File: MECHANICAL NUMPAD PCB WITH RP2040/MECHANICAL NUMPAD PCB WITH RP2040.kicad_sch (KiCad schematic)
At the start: 71 parts, among them IC2 RP2040_QFN56, J1 USB_C_Receptacle_USB2.0_16P, SW1 SW_Push, SW10 SW_Push, SW11 SW_Push, SW12 SW_Push, SW13 SW_Push, SW14 SW_Push, SW15 SW_Push, SW16 SW_Push, SW17 SW_Push, SW2 SW_Push, SW21 SKRAAKE010, SW22 SKRAAKE010, SW3 SW_Push, SW4 SW_Push, SW5 SW_Push, SW6 SW_Push, SW7 SW_Push, SW8 SW_Push, SW9 SW_Push, U2 AP2112K-3.3, U5 8MB QSPI Flash, Y1 12MHZ

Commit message: Finished PCB
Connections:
- net ROW1: now also D4.1 (K)
- net ROW2: no longer D10.1 (K), D11.1 (K), D12.1 (K), D13.1 (K), D14.1 (K), D15.1 (K), D16.1 (K), D17.1 (K), D9.1 (K)
- net ROW3: now also D10.1 (K), D11.1 (K), D12.1 (K), D9.1 (K)
- net ROW4: now also D13.1 (K), D14.1 (K), D15.1 (K), D16.1 (K)
- net ROW5: now also D17.1 (K)
- net at D4.2 (A): now also SW4.2
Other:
- moved on the sheet: C10, C11, C12, C13, C14, C15, C16, C17, C19, C20, C7, C9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

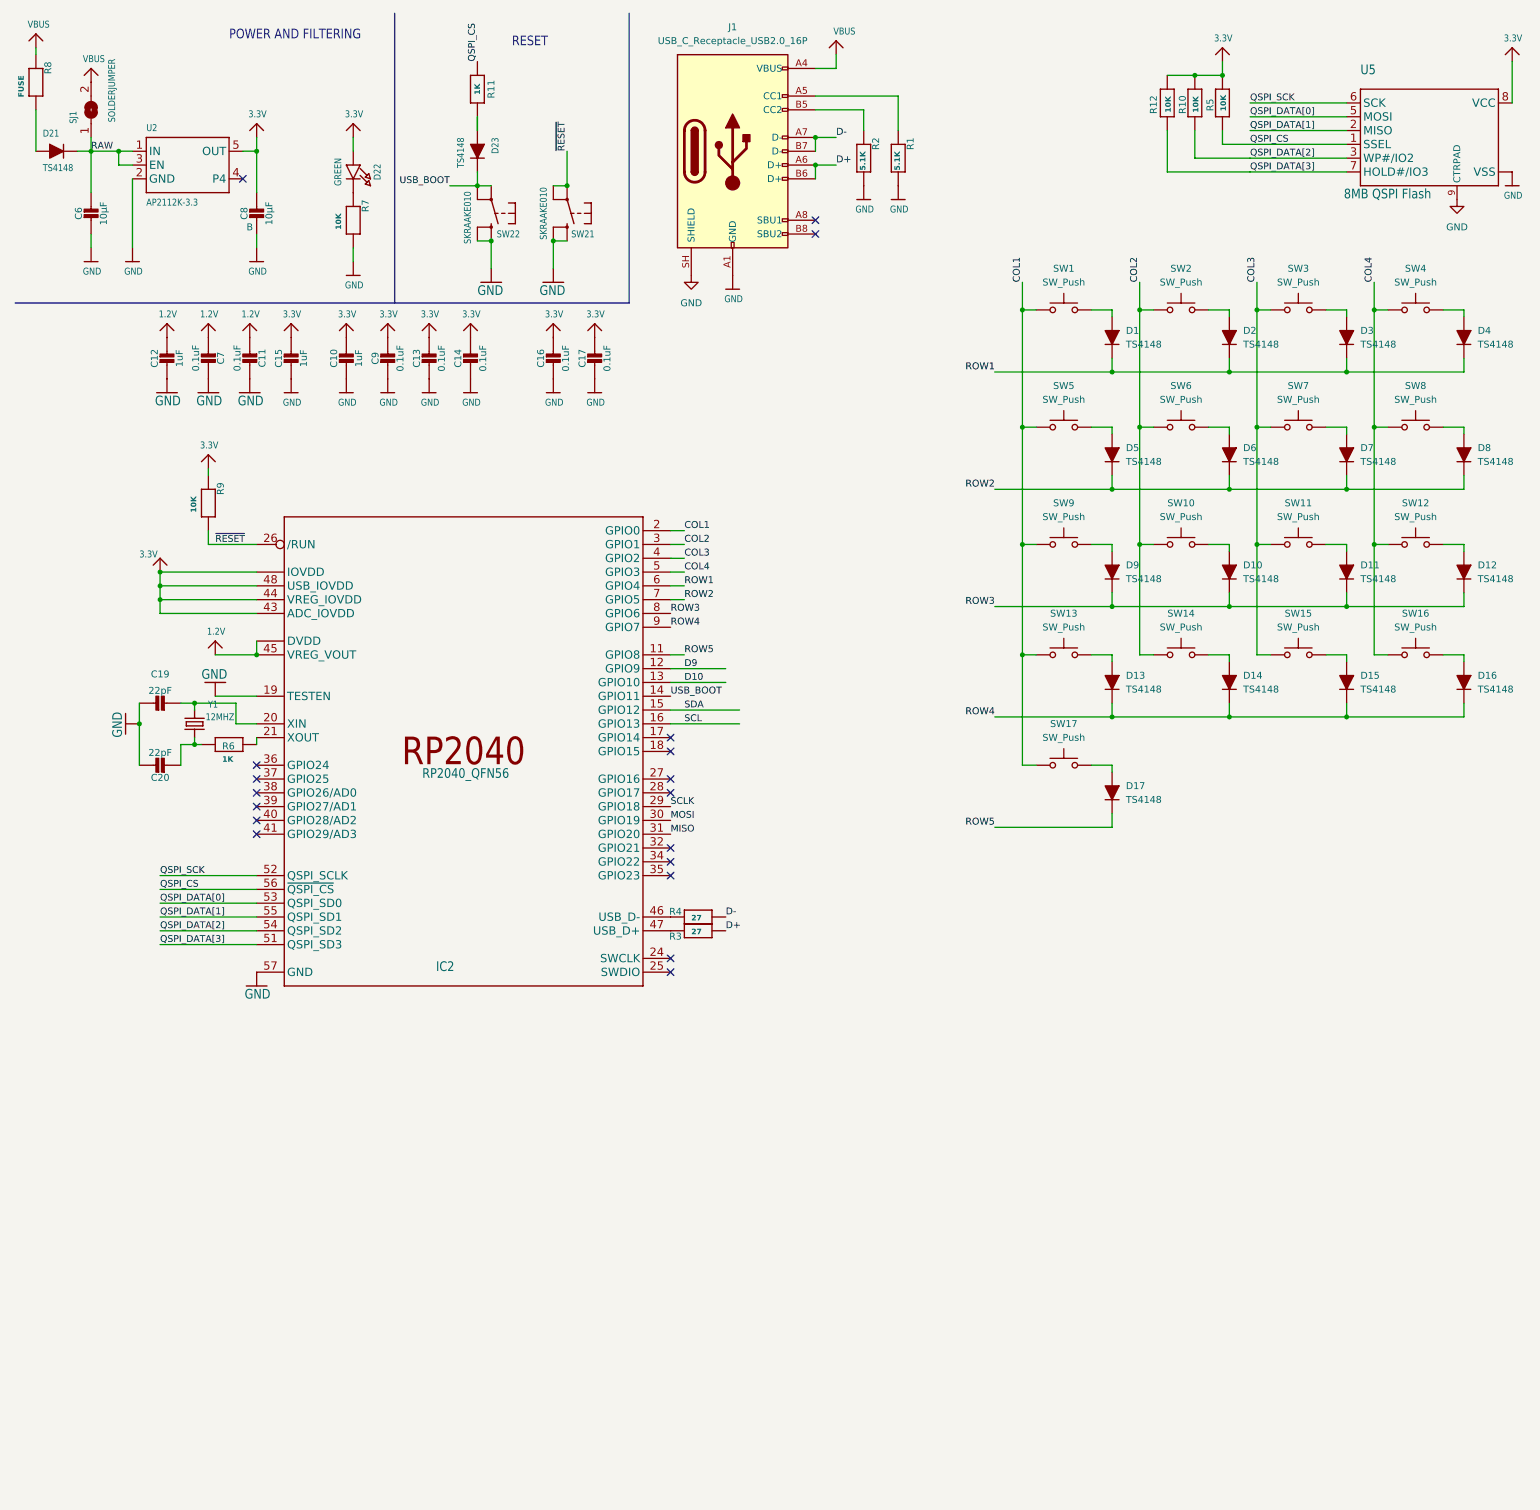
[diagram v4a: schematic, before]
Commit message: In progress of adding Neopixels
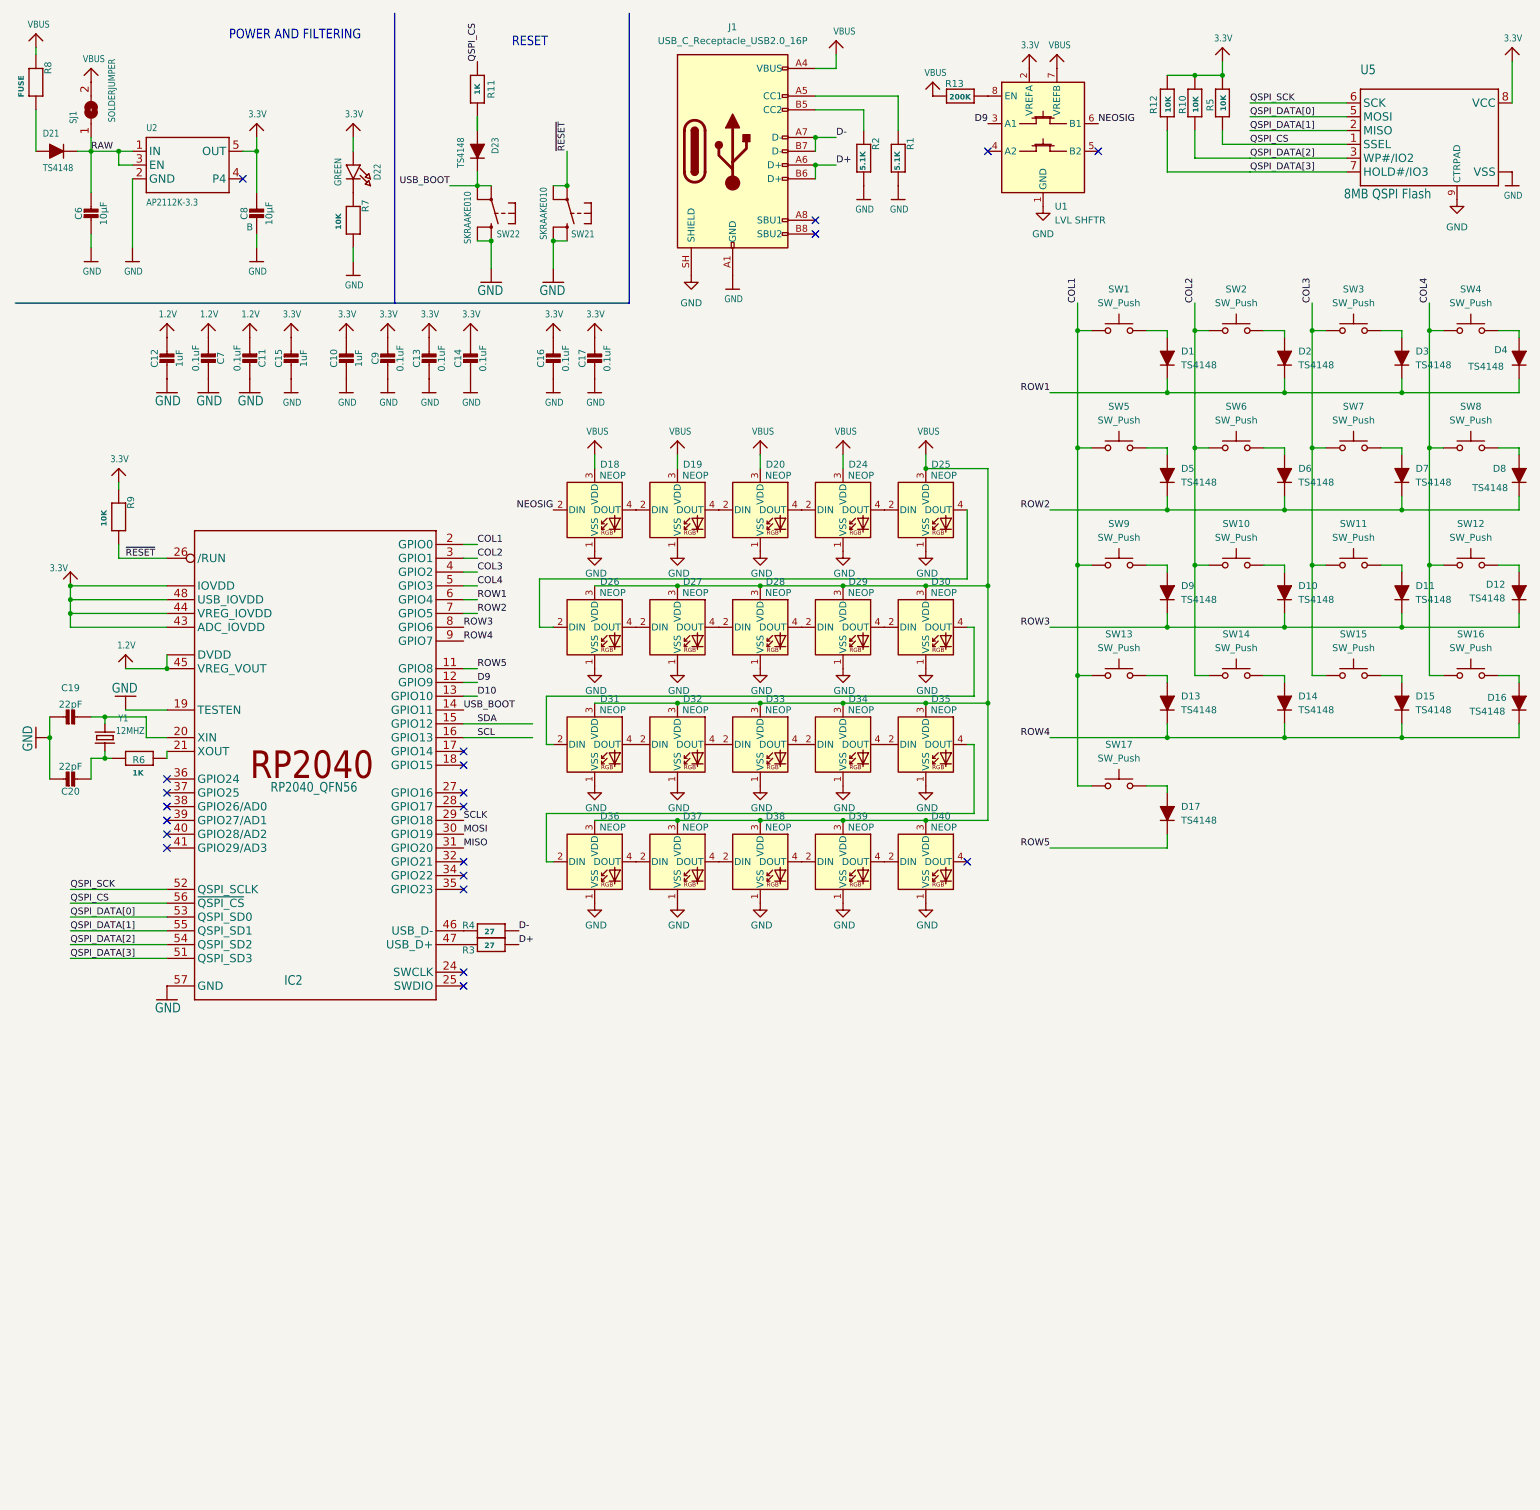
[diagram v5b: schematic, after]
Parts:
- added D18, D19, D20, D24, D25, D26, D27, D28, D29, D30, D31, D32, D33, D34, D35, D36, D37, D38, D39, D40: NEOP, LED_SMD:LED_SK6812MINI-E_3.2x2.8mm_P1.5mm_ReverseMount, symbol LED:SK6812MINI-E
- added R13: 200K, Resistor_SMD:R_0603_1608Metric, symbol Adafruit KB2040-eagle-import:RESISTOR_0402NO
- added U1: LVL SHFTR, Package_SO:VSSOP-8_2.3x2mm_P0.5mm, symbol Logic_LevelTranslator:TXS0102DCU
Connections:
- net 3.3V: now also U1.2 (VREFA)
- net D9: now also U1.3 (A1)
- net GND: now also D18.1 (VSS), D19.1 (VSS), D20.1 (VSS), D24.1 (VSS), D25.1 (VSS), D26.1 (VSS), D27.1 (VSS), D28.1 (VSS), D29.1 (VSS), D30.1 (VSS), D31.1 (VSS), D32.1 (VSS), D33.1 (VSS), D34.1 (VSS), D35.1 (VSS), D36.1 (VSS), D37.1 (VSS), D38.1 (VSS), D39.1 (VSS), D40.1 (VSS), U1.1 (GND)
- net VBUS: now also D18.3 (VDD), D19.3 (VDD), D20.3 (VDD), D24.3 (VDD), D25.3 (VDD), D26.3 (VDD), D27.3 (VDD), D28.3 (VDD), D29.3 (VDD), D30.3 (VDD), D31.3 (VDD), D32.3 (VDD), D33.3 (VDD), D34.3 (VDD), D35.3 (VDD), D36.3 (VDD), D37.3 (VDD), D38.3 (VDD), D39.3 (VDD), D40.3 (VDD), R13.1, U1.7 (VREFB)
- new net: D24.4 (DOUT), D25.2 (DIN)
- new net: D25.4 (DOUT), D26.2 (DIN)
- new net: D30.4 (DOUT), D31.2 (DIN)
- new net: D31.4 (DOUT), D32.2 (DIN)
- new net: D27.4 (DOUT), D28.2 (DIN)
- new net: D28.4 (DOUT), D29.2 (DIN)
- new net: D19.4 (DOUT), D20.2 (DIN)
- new net: D20.4 (DOUT), D24.2 (DIN)
- new net: D29.4 (DOUT), D30.2 (DIN)
- new net: D18.4 (DOUT), D19.2 (DIN)
- new net: R13.2, U1.8 (EN)
- new net: D32.4 (DOUT), D33.2 (DIN)
- new net: D33.4 (DOUT), D34.2 (DIN)
- new net: D39.4 (DOUT), D40.2 (DIN)
- new net: D34.4 (DOUT), D35.2 (DIN)
- new net: D35.4 (DOUT), D36.2 (DIN)
- new net: D38.4 (DOUT), D39.2 (DIN)
- new net: D26.4 (DOUT), D27.2 (DIN)
- new net: D36.4 (DOUT), D37.2 (DIN)
- new net: D37.4 (DOUT), D38.2 (DIN)
- new net NEOSIG: D18.2 (DIN), U1.6 (B1)
- no-connect marks 18 -> 21
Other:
- moved on the sheet: C19, C20, D1, D10, D11, D12, D13, D14, D15, D16, D17, D2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

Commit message: Generating Gerbers and refining PCBs
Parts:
- U1: footprint Package_SO:VSSOP-8_2.3x2mm_P0.5mm -> Package_DFN_QFN:Texas_S-PVQFN-N14; symbol Logic_LevelTranslator:TXS0102DCU -> Logic_LevelTranslator:TXB0104RGY
- renumbered D18 to D31, D19 to D32, D20 to D33, D24 to D34, D25 to D35, D26 to D36, D27 to D37, D28 to D38, D29 to D39, D30 to D40, D31 to D41, D32 to D42, D33 to D43, D34 to D44, D35 to D45, D36 to D46, D37 to D47, D38 to D48, D39 to D49, D40 to D50
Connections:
- net 3.3V: now also R13.1, U1.1 (VCCA); no longer U1.2 (VREFA)
- net D9: now also U1.2 (A1); no longer U1.3 (A1)
- net GND: now also U1.15 (Pad), U1.7 (GND); no longer U1.1 (GND)
- net NEOSIG: now also U1.13 (B1); no longer U1.6 (B1)
- net VBUS: now also U1.14 (VCCB); no longer R13.1, U1.7 (VREFB)
- no-connect marks 21 -> 19
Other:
- moved on the sheet: D31, D32, D33, D34, D35, D36, D37, D38, D39, D40, D41, D42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
